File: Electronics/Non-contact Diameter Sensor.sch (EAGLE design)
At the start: 11 parts

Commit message: Eliminated ground pour islands and reduced size of blank areas by moving traces. Moved J6 onto board a bit better.
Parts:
- renumbered J2 to PWR, J3 to I2C, J4 to LASER
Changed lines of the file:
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@@
 <part name="ARDUINO_NANO1" library="ArduinoNanoV30" deviceset="ARDUINO_NANO" device=""/>
 <part name="J1" library="SparkFun-Connectors" library_urn="urn:adsk.eagle:library:513" deviceset="CONN_02" device="" package3d_urn="urn:adsk.eagle:package:38039/1"/>
-<part name="J2" library="SparkFun-Connectors" library_urn="urn:adsk.eagle:library:513" deviceset="CONN_02" device="3.5MM" package3d_urn="urn:adsk.eagle:package:38050/1"/>
-<part name="J3" library="SparkFun-Connectors" library_urn="urn:adsk.eagle:library:513" deviceset="CONN_02" device="3.5MM" package3d_urn="urn:adsk.eagle:package:38050/1"/>
-<part name="J4" library="SparkFun-Connectors" library_urn="urn:adsk.eagle:library:513" deviceset="CONN_02" device="3.5MM" package3d_urn="urn:adsk.eagle:package:38050/1"/>
+<part name="PWR" library="SparkFun-Connectors" library_urn="urn:adsk.eagle:library:513" deviceset="CONN_02" device="3.5MM" package3d_urn="urn:adsk.eagle:package:38050/1"/>
+<part name="I2C" library="SparkFun-Connectors" library_urn="urn:adsk.eagle:library:513" deviceset="CONN_02" device="3.5MM" package3d_urn="urn:adsk.eagle:package:38050/1"/>
+<part name="LASER" library="SparkFun-Connectors" library_urn="urn:adsk.eagle:library:513" deviceset="CONN_02" device="3.5MM" package3d_urn="urn:adsk.eagle:package:38050/1"/>
 <part name="J5" library="SparkFun-Connectors" library_urn="urn:adsk.eagle:library:513" deviceset="CONN_07" device="" package3d_urn="urn:adsk.eagle:package:38129/1"/>
 <part name="J6" library="SparkFun-Connectors" library_urn="urn:adsk.eagle:library:513" deviceset="CONN_07" device="" package3d_urn="urn:adsk.eagle:package:38129/1"/>
@@
 <attribute name="NAME" x="-25.4" y="13.208" size="1.778" layer="95" font="vector"/>
 </instance>
-<instance part="J2" gate="G$1" x="109.22" y="66.04" smashed="yes" rot="R180">
+<instance part="PWR" gate="G$1" x="109.22" y="66.04" smashed="yes" rot="R180">
 <attribute name="VALUE" x="111.76" y="70.866" size="1.778" layer="96" font="vector" rot="R180"/>
 <attribute name="NAME" x="111.76" y="60.452" size="1.778" layer="95" font="vector" rot="R180"/>
 </instance>
-<instance part="J3" gate="G$1" x="109.22" y="43.18" smashed="yes" rot="R180">
+<instance part="I2C" gate="G$1" x="109.22" y="43.18" smashed="yes" rot="R180">
 <attribute name="VALUE" x="111.76" y="48.006" size="1.778" layer="96" font="vector" rot="R180"/>
 <attribute name="NAME" x="111.76" y="37.592" size="1.778" layer="95" font="vector" rot="R180"/>
 </instance>
-<instance part="J4" gate="G$1" x="109.22" y="55.88" smashed="yes" rot="R180">
+<instance part="LASER" gate="G$1" x="109.22" y="55.88" smashed="yes" rot="R180">
 <attribute name="VALUE" x="111.76" y="60.706" size="1.778" layer="96" font="vector" rot="R180"/>
 <attribute name="NAME" x="111.76" y="50.292" size="1.778" layer="95" font="vector" rot="R180"/>
@@
 <net name="GND" class="0">
 <segment>
-<pinref part="J4" gate="G$1" pin="1"/>
+<pinref part="LASER" gate="G$1" pin="1"/>
 <wire x1="101.6" y1="55.88" x2="63.5" y2="55.88" width="0.1524" layer="91"/>
-<pinref part="J2" gate="G$1" pin="2"/>
+<pinref part="PWR" gate="G$1" pin="2"/>
 <wire x1="101.6" y1="63.5" x2="88.9" y2="63.5" width="0.1524" layer="91"/>
 <wire x1="88.9" y1="63.5" x2="63.5" y2="63.5" width="0.1524" layer="91"/>
@@
 <net name="LASER" class="0">
 <segment>
-<pinref part="J4" gate="G$1" pin="2"/>
+<pinref part="LASER" gate="G$1" pin="2"/>
 <wire x1="101.6" y1="53.34" x2="76.2" y2="53.34" width="0.1524" layer="91"/>
 <wire x1="76.2" y1="53.34" x2="76.2" y2="45.72" width="0.1524" layer="91"/>
 <pinref part="ARDUINO_NANO1" gate="G$1" pin="A6"/>
 <wire x1="76.2" y1="45.72" x2="58.42" y2="45.72" width="0.1524" layer="91"/>
+<label x="88.9" y="53.34" size="1.778" layer="95"/>
 </segment>
 </net>
@@
 <pinref part="ARDUINO_NANO1" gate="G$1" pin="VIN"/>
 <wire x1="58.42" y1="58.42" x2="58.42" y2="66.04" width="0.1524" layer="91"/>
-<pinref part="J2" gate="G$1" pin="1"/>
+<pinref part="PWR" gate="G$1" pin="1"/>
 <wire x1="58.42" y1="66.04" x2="93.98" y2="66.04" width="0.1524" layer="91"/>
 <wire x1="93.98" y1="66.04" x2="101.6" y2="66.04" width="0.1524" layer="91"/>
@@
 <pinref part="ARDUINO_NANO1" gate="G$1" pin="A5"/>
 <wire x1="101.6" y1="43.18" x2="58.42" y2="43.18" width="0.1524" layer="91"/>
-<pinref part="J3" gate="G$1" pin="1"/>
+<pinref part="I2C" gate="G$1" pin="1"/>
 <label x="91.44" y="43.18" size="1.778" layer="95"/>
 </segment>
@@
 <pinref part="ARDUINO_NANO1" gate="G$1" pin="A4"/>
 <wire x1="101.6" y1="40.64" x2="58.42" y2="40.64" width="0.1524" layer="91"/>
-<pinref part="J3" gate="G$1" pin="2"/>
+<pinref part="I2C" gate="G$1" pin="2"/>
 <label x="91.44" y="40.64" size="1.778" layer="95"/>
 </segment>

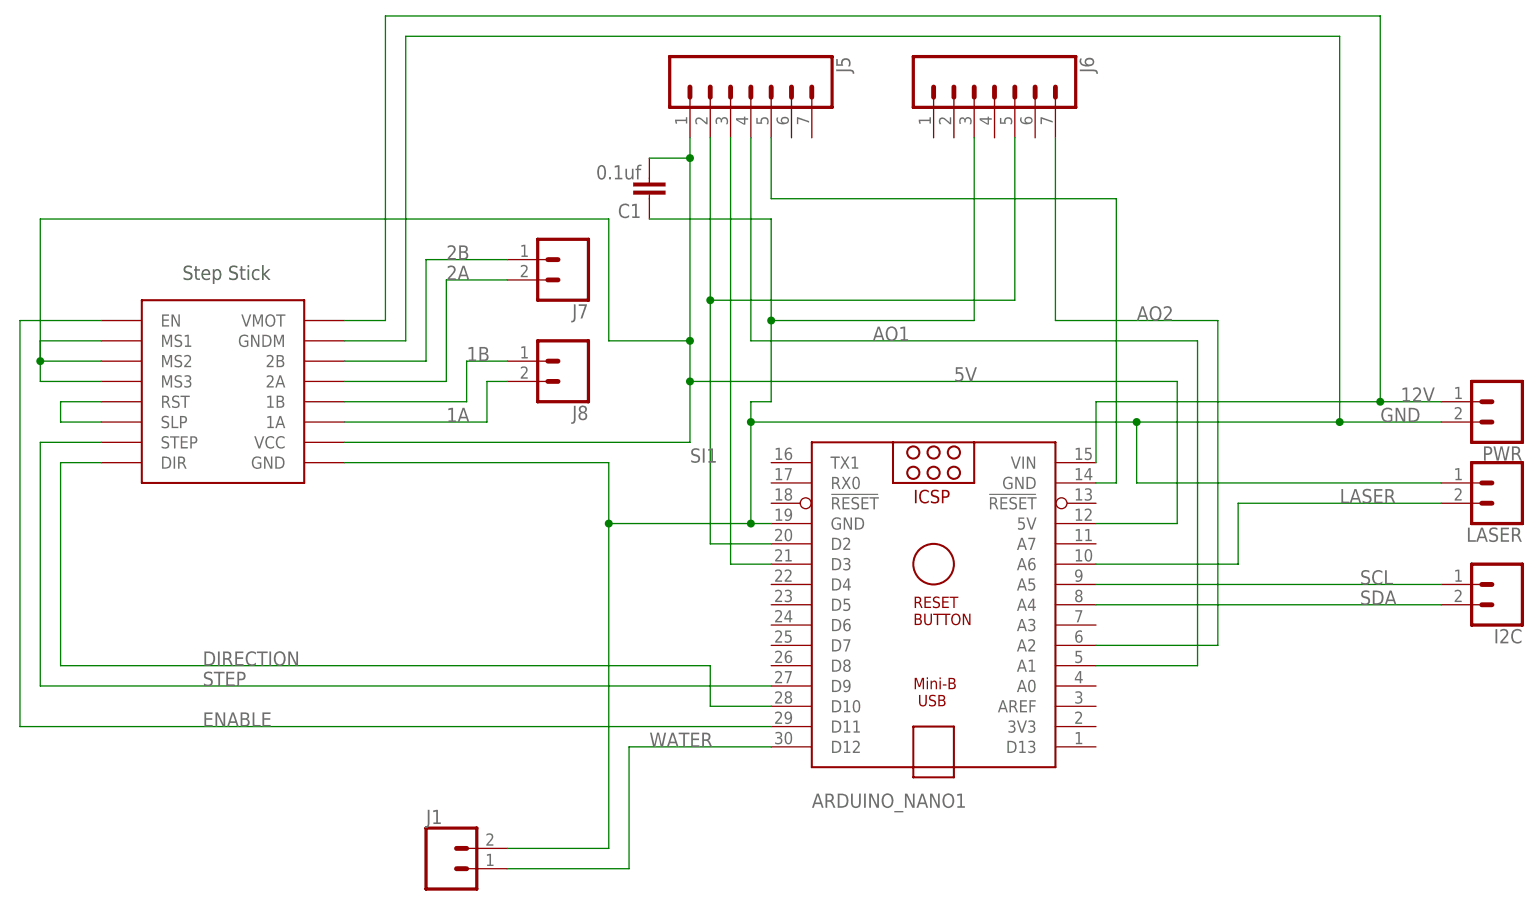
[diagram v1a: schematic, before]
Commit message: Redesigned the electronics board. Made the necessary changes in the pin assignments in the code. Updated image in the BOM.
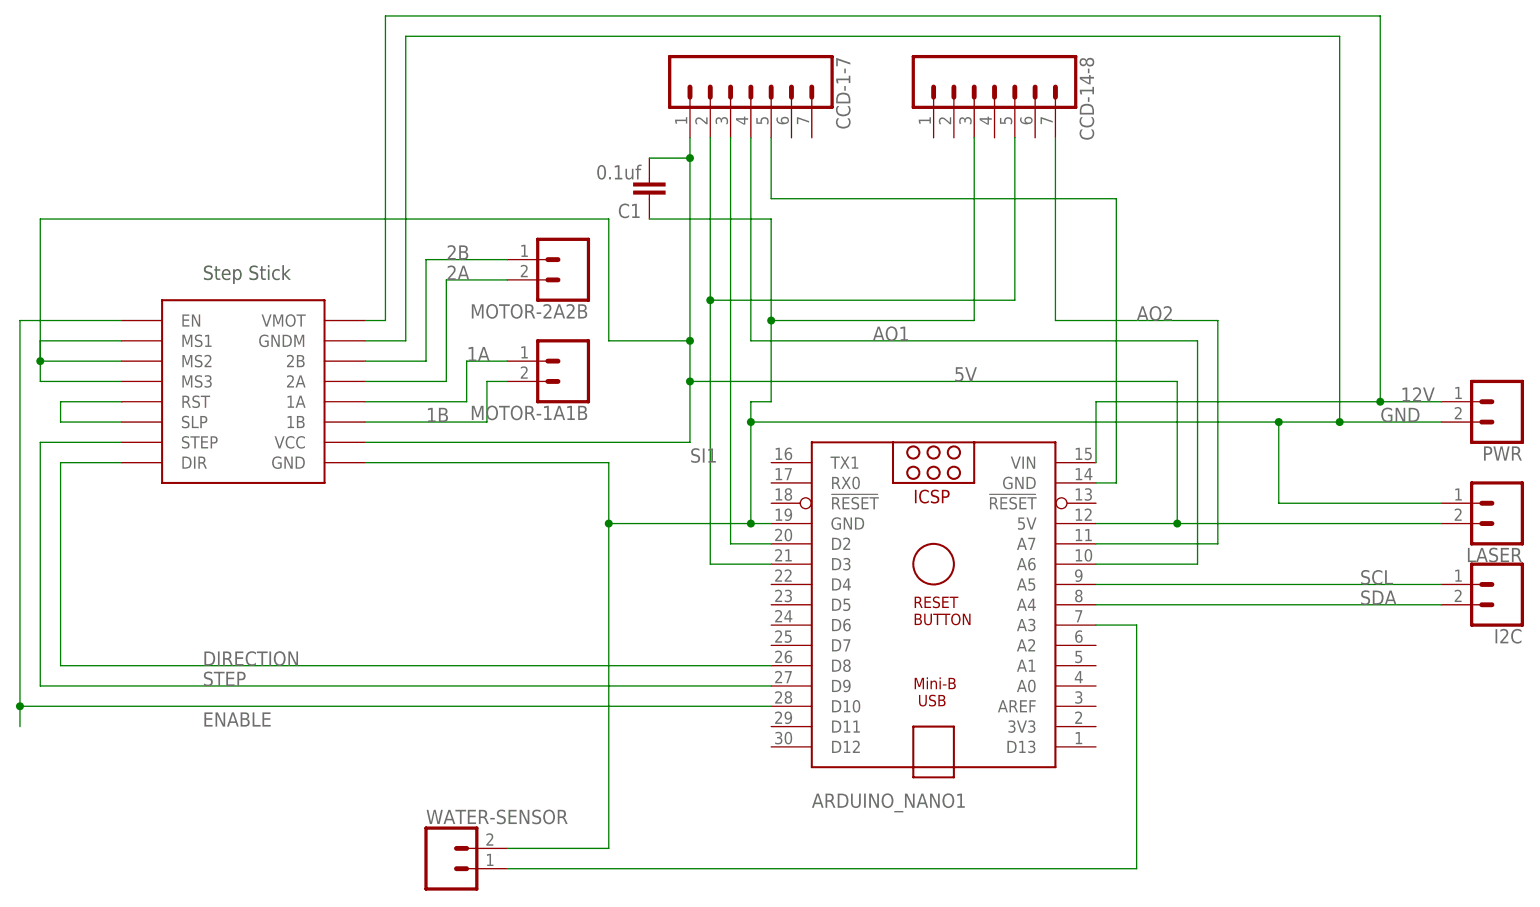
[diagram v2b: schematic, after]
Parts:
- renumbered J1 to WATER-SENSOR, J5 to CCD-1-7, J6 to CCD-14-8, J7 to MOTOR-2A2B, J8 to MOTOR-1A1B
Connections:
- removed net LASER: ARDUINO_NANO1.A6, LASER.2
- removed net WATER: ARDUINO_NANO1.D12, WATER-SENSOR.1
- new net N$1: ARDUINO_NANO1.A3, WATER-SENSOR.1
- net 1A: now also MOTOR-1A1B.1; no longer MOTOR-1A1B.2
- net 1B: now also MOTOR-1A1B.2; no longer MOTOR-1A1B.1
- net 5V: now also LASER.2
- net AO1: now also ARDUINO_NANO1.A6; no longer ARDUINO_NANO1.A1
- net AO2: now also ARDUINO_NANO1.A7; no longer ARDUINO_NANO1.A2
- net CLK: now also ARDUINO_NANO1.D2; no longer ARDUINO_NANO1.D3
- net DIRECTION: now also ARDUINO_NANO1.D8; no longer ARDUINO_NANO1.D10
- net ENABLE: now also ARDUINO_NANO1.D10; no longer ARDUINO_NANO1.D11
- net SI1: now also ARDUINO_NANO1.D3; no longer ARDUINO_NANO1.D2
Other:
- moved on the sheet: LASER
